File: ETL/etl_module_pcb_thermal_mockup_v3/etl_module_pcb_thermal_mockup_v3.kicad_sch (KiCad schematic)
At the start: 25 parts, among them J3 Conn_02x05_Counter_Clockwise, U1 ETROC_dummy_thermal_sensors, U2 ETROC_dummy_thermal_sensors, U3 ETROC_dummy_thermal_sensors, U4 ETROC_dummy_thermal_sensors, U5 ADC088SO22, U6 ADC088SO22, U7 ADC088SO22, U8 ADC088SO22

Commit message: Progress on etl_module_pcb_thermal_mockup_v3
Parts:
- removed C1, C3, C5, C7: 1.0uF, Capacitor_SMD:C_0201_0603Metric_Pad0.64x0.40mm_HandSolder, symbol Device:C
- removed C2, C4, C6, C8: 0.1uF, Capacitor_SMD:C_0201_0603Metric_Pad0.64x0.40mm_HandSolder, symbol Device:C
- removed RN1, RN2, RN3, RN4: 10k, Resistor_SMD:R_Array_Convex_8x0602, symbol Device:R_Pack08
- removed U5, U6, U7, U8: ADC088SO22, Package_SO:TSSOP-16_4.4x5mm_P0.65mm, symbol unl_silab:ADC088SO22
- added C?: 1uF, symbol Device:C
- added R? (x10): 40k, symbol Device:R
- added R?: 1M, symbol Device:R
- added RV?: 25k, symbol Device:R_Potentiometer
- added U?: AD780, Package_SO:SOIC-8_3.9x4.9mm_P1.27mm, symbol unl_silab:AD780
- added U?: AD77x8, Package_SO:SOIC-28W_7.5x18.7mm_P1.27mm, symbol unl_silab:AD77x8
- added Y?: 32kHz, symbol Device:Crystal
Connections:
- net +5V: now also C?.1, R?.1, R?.1, R?.1, R?.1, R?.1, R?.1, R?.1, R?.1, R?.1, U?.2 (+V_{IN}), U?.26 (DV_{DD}), U?.3 (AV_{DD})
- net CLK: now also U?.20 (SCLK)
- net DIN: now also U?.24 (DIN)
- net DOUT: now also U?.23 (DOUT)
- net GND: now also U1.11 (LGAD_BL+), U1.3 (ETROC_BLp), U2.11 (LGAD_BL+), U2.3 (ETROC_BLp), U3.11 (LGAD_BL+), U3.3 (ETROC_BLp), U4.11 (LGAD_BL+), U4.3 (ETROC_BLp), C?.2, R?.2, RV?.1, U?.14 (REFIN2(-)/AIN10), U?.17 (AGND), U?.25 (DGND), U?.4 (AGND), U?.4 (GND), U?.5 (REFIN1(-)); no longer U1.105 (LGAD_BR-), U1.108 (ETROC_TR-), U1.119 (ETROC_BR-), U1.12 (LGAD_BL-), U1.23 (LGAD_TL-), U1.5 (ETROC_BL-), U1.83 (LGAD_TR-), U1.9 (ETROC_TL-), U2.105 (LGAD_BR-), U2.108 (ETROC_TR-), U2.119 (ETROC_BR-), U2.12 (LGAD_BL-), U2.23 (LGAD_TL-), U2.5 (ETROC_BL-), U2.83 (LGAD_TR-), U2.9 (ETROC_TL-), U3.105 (LGAD_BR-), U3.108 (ETROC_TR-), U3.119 (ETROC_BR-), U3.12 (LGAD_BL-), U3.23 (LGAD_TL-), U3.5 (ETROC_BL-), U3.83 (LGAD_TR-), U3.9 (ETROC_TL-), U4.105 (LGAD_BR-), U4.108 (ETROC_TR-), U4.119 (ETROC_BR-), U4.12 (LGAD_BL-), U4.23 (LGAD_TL-), U4.5 (ETROC_BL-), U4.83 (LGAD_TR-), U4.9 (ETROC_TL-)
- net VCC: now also U3.1 (VCC), U4.1 (VCC); no longer U3.121 (VSS), U4.121 (VSS)
- net VSS: now also U3.121 (VSS), U4.121 (VSS); no longer U3.1 (VCC), U4.1 (VCC)
- net LGAD3: now reaches U3.104 (LGAD_BR+)
- net LGAD3: now also U3.83 (LGAD_TR-), U?.15 (AIN6)
- net at U3.107 (ETROC_TR+): now also U3.9 (ETROC_TL-)
- net ETROC3: now reaches U3.117 (ETROC_BR+)
- net ETROC3: now also U3.108 (ETROC_TR-), U?.11 (AIN5)
- net at U3.21 (LGAD_TL+): now also U3.12 (LGAD_BL-)
- net at U3.8 (ETROC_TL+): now also U3.5 (ETROC_BL-)
- net at U3.81 (LGAD_TR+): now also U3.23 (LGAD_TL-)
- net at U1.104 (LGAD_BR+): now also U1.83 (LGAD_TR-)
- net at U1.117 (ETROC_BR+): now also U1.108 (ETROC_TR-)
- net at U1.81 (LGAD_TR+): now also U1.23 (LGAD_TL-)
- net at U1.107 (ETROC_TR+): now also U1.9 (ETROC_TL-)
- net at U1.21 (LGAD_TL+): now also U1.12 (LGAD_BL-)
- net at U1.8 (ETROC_TL+): now also U1.5 (ETROC_BL-)
- net LGAD2: now reaches U2.104 (LGAD_BR+)
- net LGAD2: now also U2.83 (LGAD_TR-), U?.10 (AIN4)
- net ETROC2: now reaches U2.117 (ETROC_BR+)
- net ETROC2: now also U2.108 (ETROC_TR-), U?.9 (AIN3)
- net at U2.81 (LGAD_TR+): now also U2.23 (LGAD_TL-)
- net at U2.107 (ETROC_TR+): now also U2.9 (ETROC_TL-)
- net at U2.21 (LGAD_TL+): now also U2.12 (LGAD_BL-)
- net at U2.8 (ETROC_TL+): now also U2.5 (ETROC_BL-)
- net LGAD4: now reaches U4.104 (LGAD_BR+)
- net LGAD4: now also U4.83 (LGAD_TR-), U?.2 (AIN8)
- net ETROC4: now reaches U4.117 (ETROC_BR+)
- net ETROC4: now also U4.108 (ETROC_TR-), U?.1 (AIN7)
- net at U4.81 (LGAD_TR+): now also U4.23 (LGAD_TL-)
- net at U4.107 (ETROC_TR+): now also U4.9 (ETROC_TL-)
- net at U4.21 (LGAD_TL+): now also U4.12 (LGAD_BL-)
- net at U4.8 (ETROC_TL+): now also U4.5 (ETROC_BL-)
- net CS1: no longer names the net of J3.4 (Pin_4)
- net CS2 renamed ~{RDY}
- net ~{RDY}: now also U?.22 (~{RDY})
- net CS3 renamed ~{RESET}
- net ~{RESET}: now also U?.19 (~{RESET})
- net CS4 renamed CS
- net CS: now also U?.21 (~{CS})
- new net: R?.2, U3.105 (LGAD_BR-)
- new net: R?.2, U3.119 (ETROC_BR-)
- new net: R?.2, RV?.2
- new net: R?.2, U2.105 (LGAD_BR-)
- new net: R?.2, U2.119 (ETROC_BR-)
- new net: R?.2, U4.105 (LGAD_BR-)
- new net: R?.2, U4.119 (ETROC_BR-)
- new net: U?.27 (XTAL2), Y?.1
- new net: U?.28 (XTAL1), Y?.2
- new net 2.5V: R?.1, RV?.3, U?.13 (REFIN2(+)/AIN9), U?.5 (TRIM)
- new net ETROC1: R?.2, U1.119 (ETROC_BR-), U?.7 (AIN1)
- new net LGAD1: R?.2, U1.105 (LGAD_BR-), U?.8 (AIN2)
- new net V_{ref}: R?.1, R?.2, U?.12 (AINCOM), U?.6 (REFIN1(+))
- no-connect marks 0 -> 6
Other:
- note added: "*(Optional)* Populate 2.5V reference for absolute (vs ratiometric)measurements."
- note added: "Single Resistance: R = 34.6 * T [C] + 9600 Four in Series: R_{ser} = 4*R = 138.4 * T [C] + 38400 V_{sense} = V * (R_{ser} / (R_{ser} + 40k)) -> 4.5mV/[C] near T=0 [C]"
- note removed: "TODO: Wire up power to pin header Wire up power to b2b connector Wire up readout to pin header Wier up readout to b2b connector Add pin header for ETROC heater power supply"
- moved on the sheet: U1, U2, U3, U4

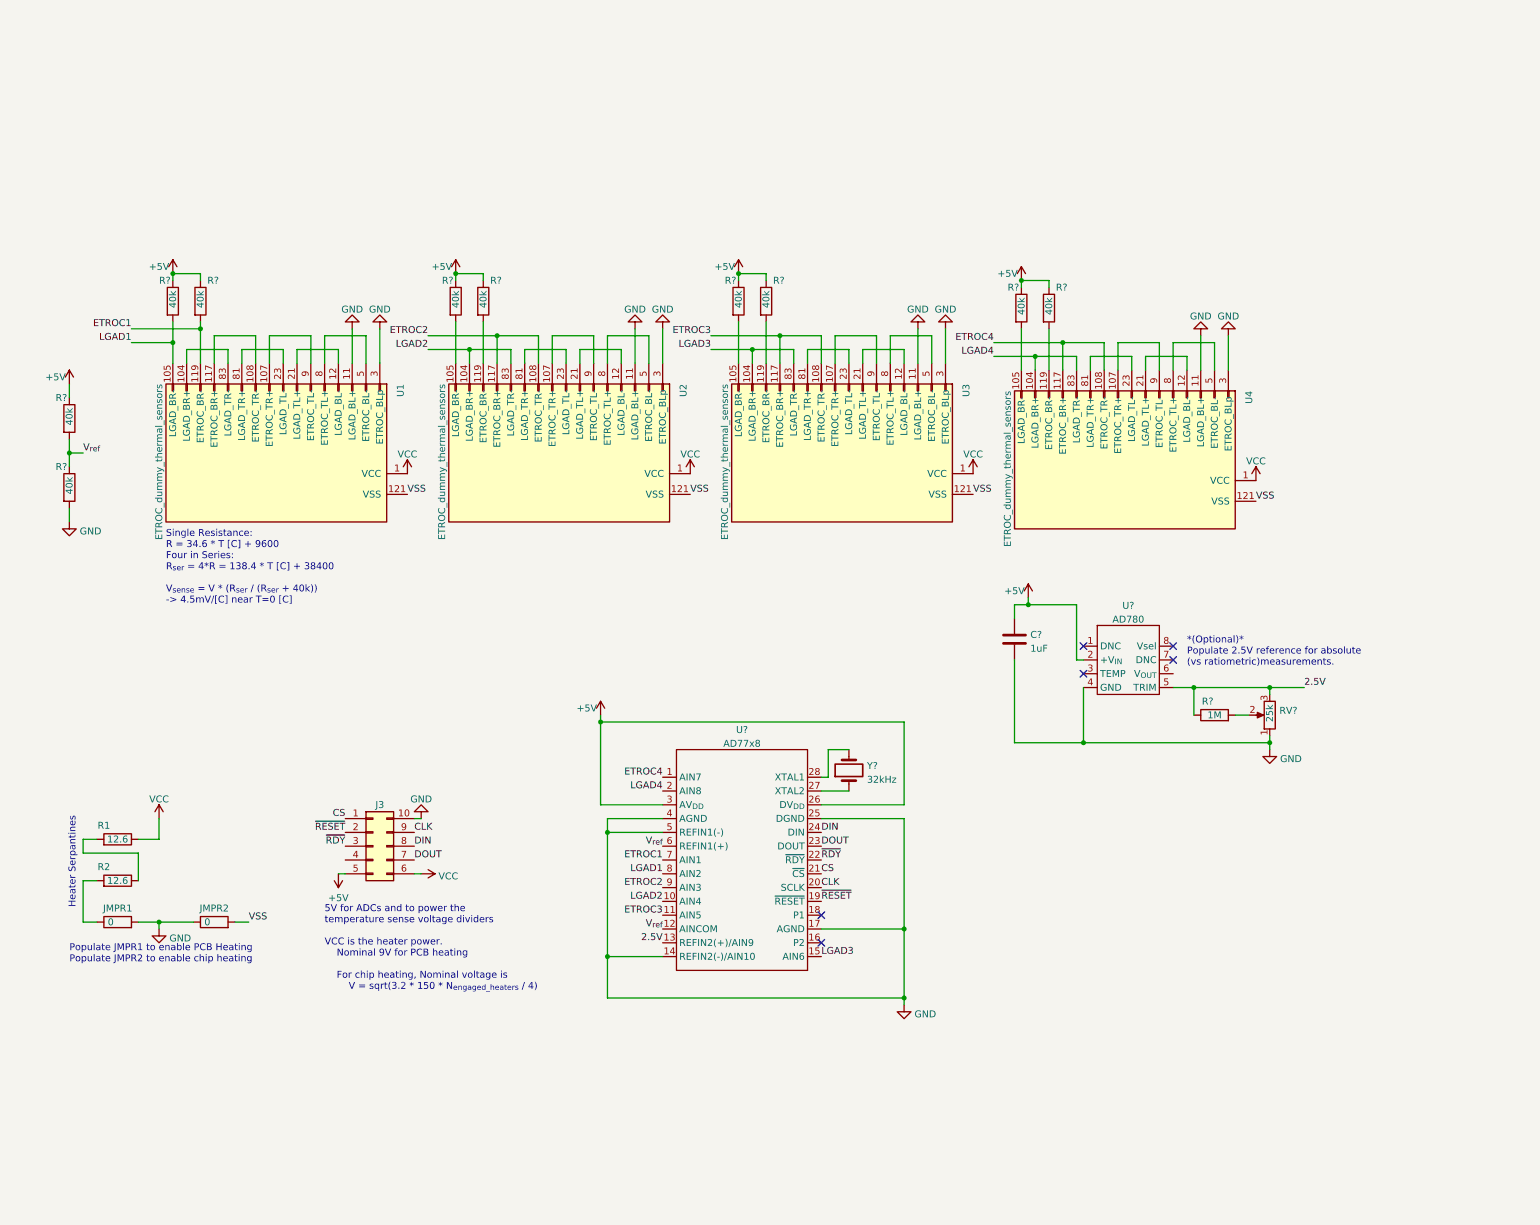
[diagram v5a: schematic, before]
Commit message: Work on etl_module_pcb_thermal_mockup_v3
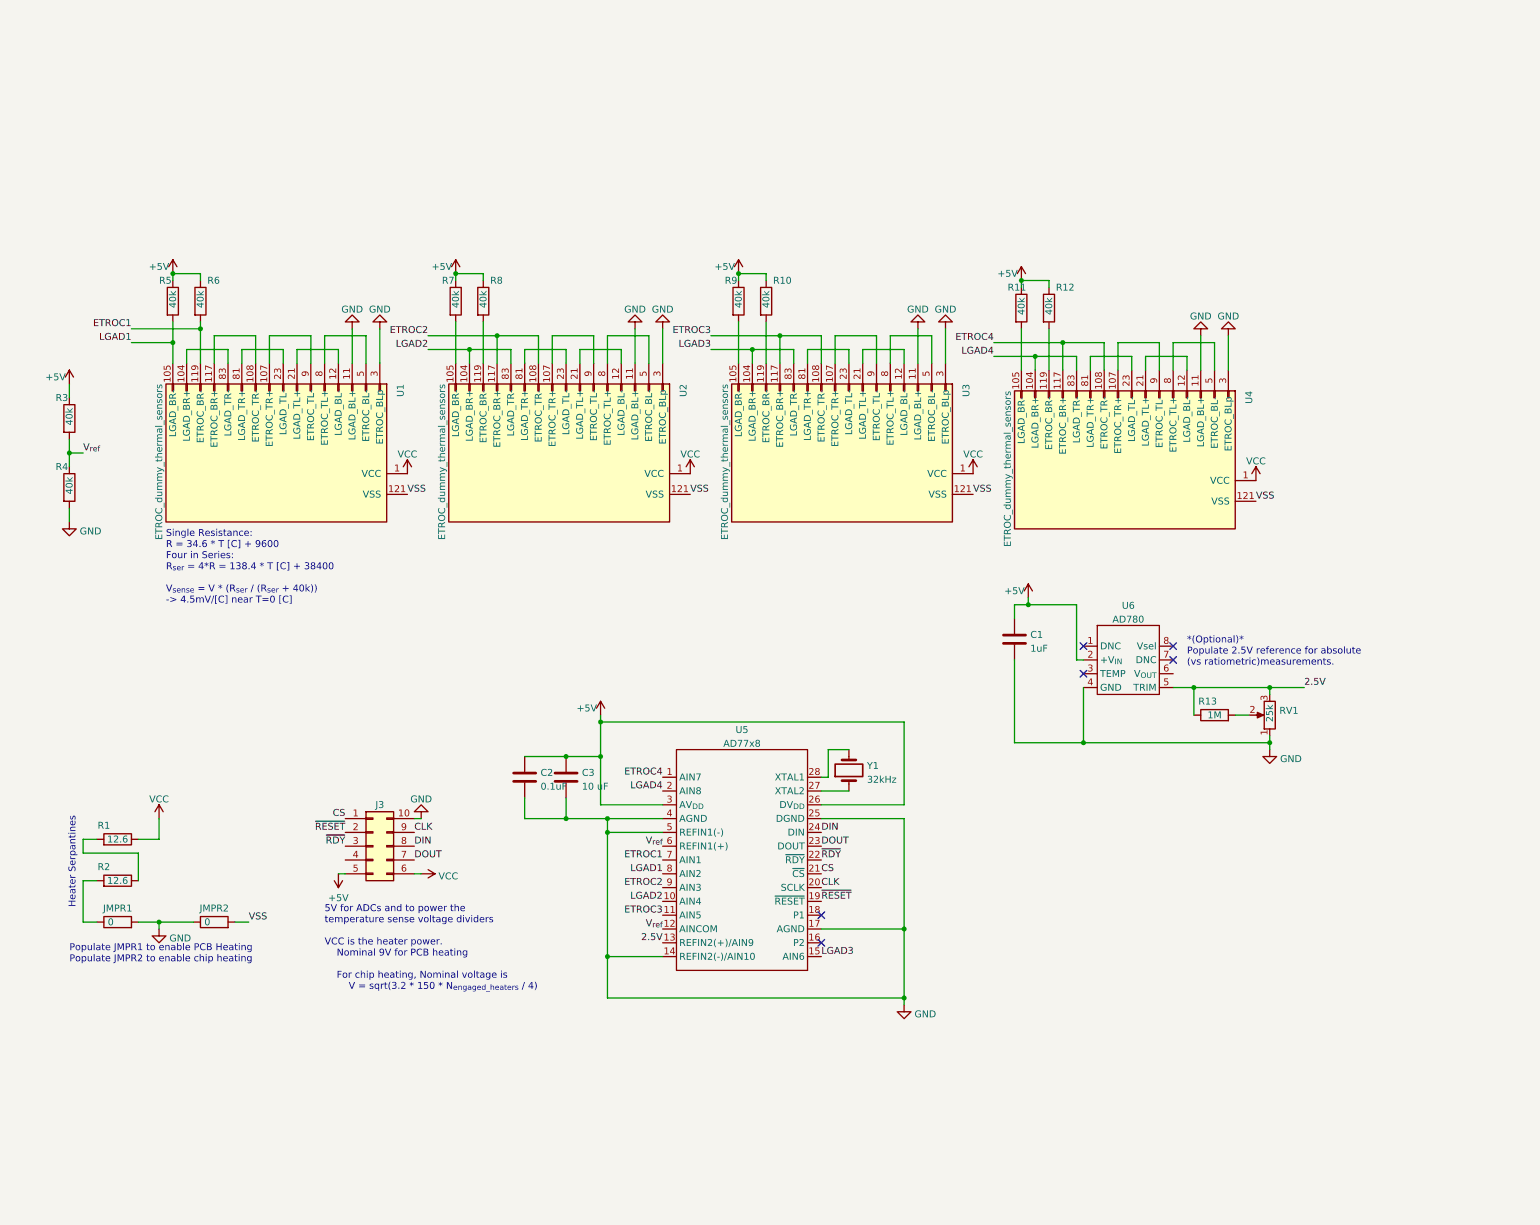
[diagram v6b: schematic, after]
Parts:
- added C2: 0.1uF, Capacitor_SMD:C_0805_2012Metric_Pad1.18x1.45mm_HandSolder, symbol Device:C
- added C3: 10 uF, Capacitor_SMD:C_0805_2012Metric_Pad1.18x1.45mm_HandSolder, symbol Device:C
- C1: renamed from C?; footprint (none) -> Capacitor_SMD:C_0805_2012Metric_Pad1.18x1.45mm_HandSolder
- R10, R11, R12, R13, R3, R4, R5, R6, R7, R8, R9: renamed from R?; footprint (none) -> Resistor_SMD:R_0805_2012Metric_Pad1.20x1.40mm_HandSolder
- RV1: renamed from RV?; footprint (none) -> Potentiometer_SMD:Potentiometer_Bourns_3224W_Vertical
- Y1: renamed from Y?; footprint (none) -> Crystal:Crystal_SMD_3215-2Pin_3.2x1.5mm
- gave numbers to parts that had none: 2
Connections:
- net +5V: now also C2.1, C3.1
- net GND: now also C2.2, C3.2

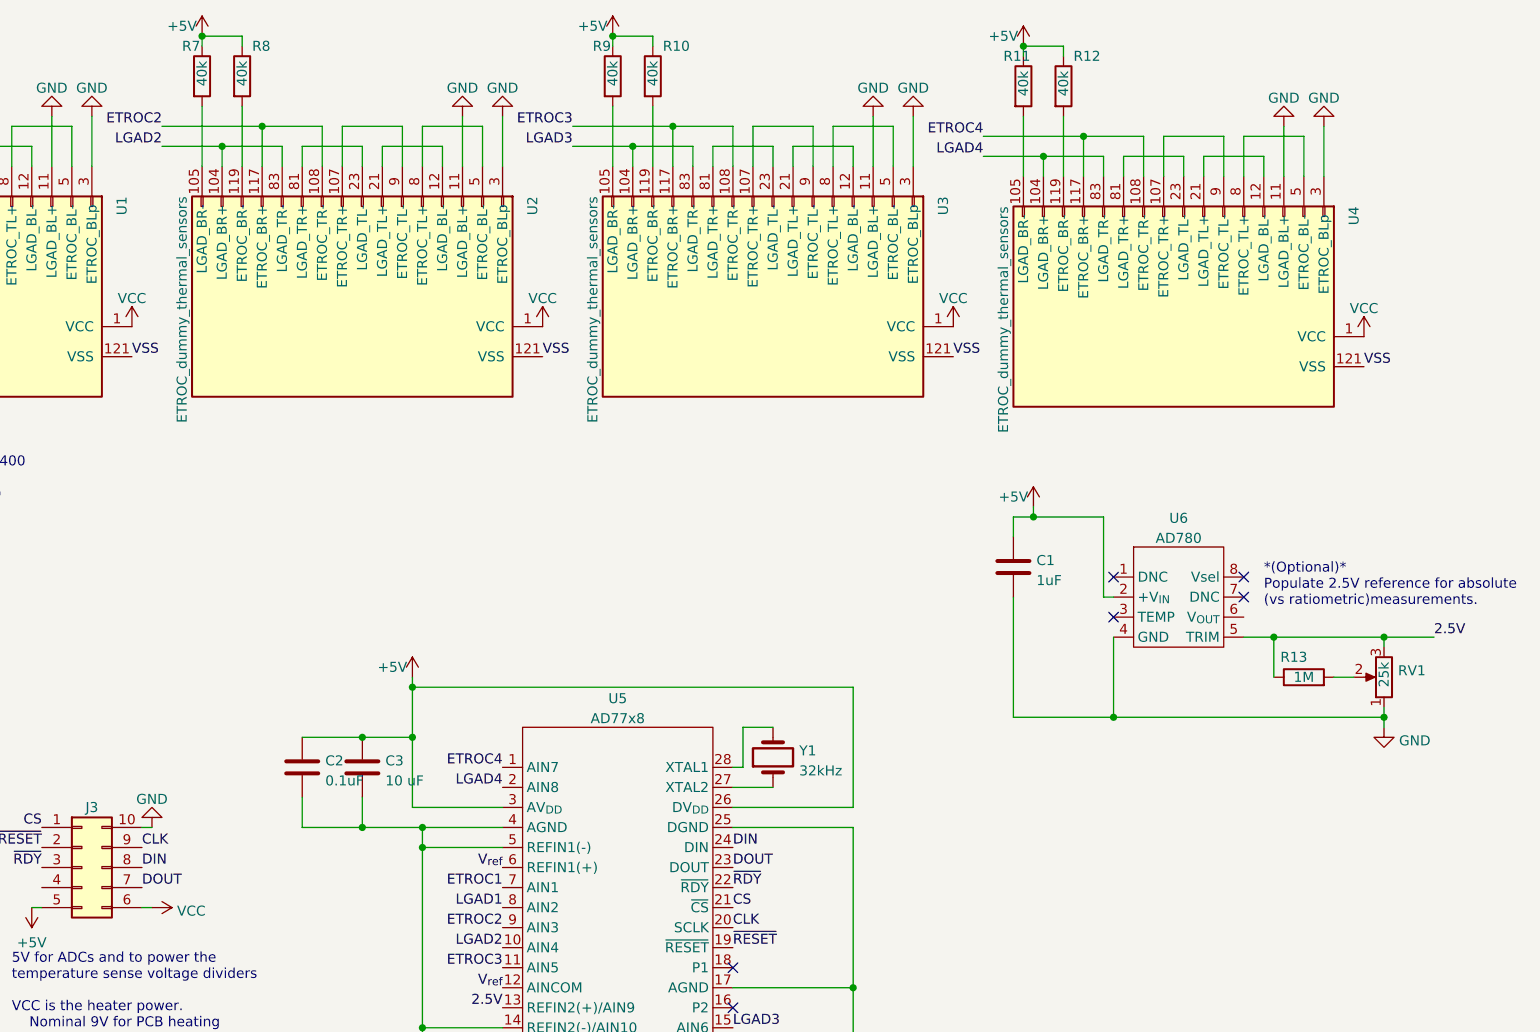
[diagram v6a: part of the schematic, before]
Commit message: Almost finished routing on etl_module_pcb_thermal_mockup_v3
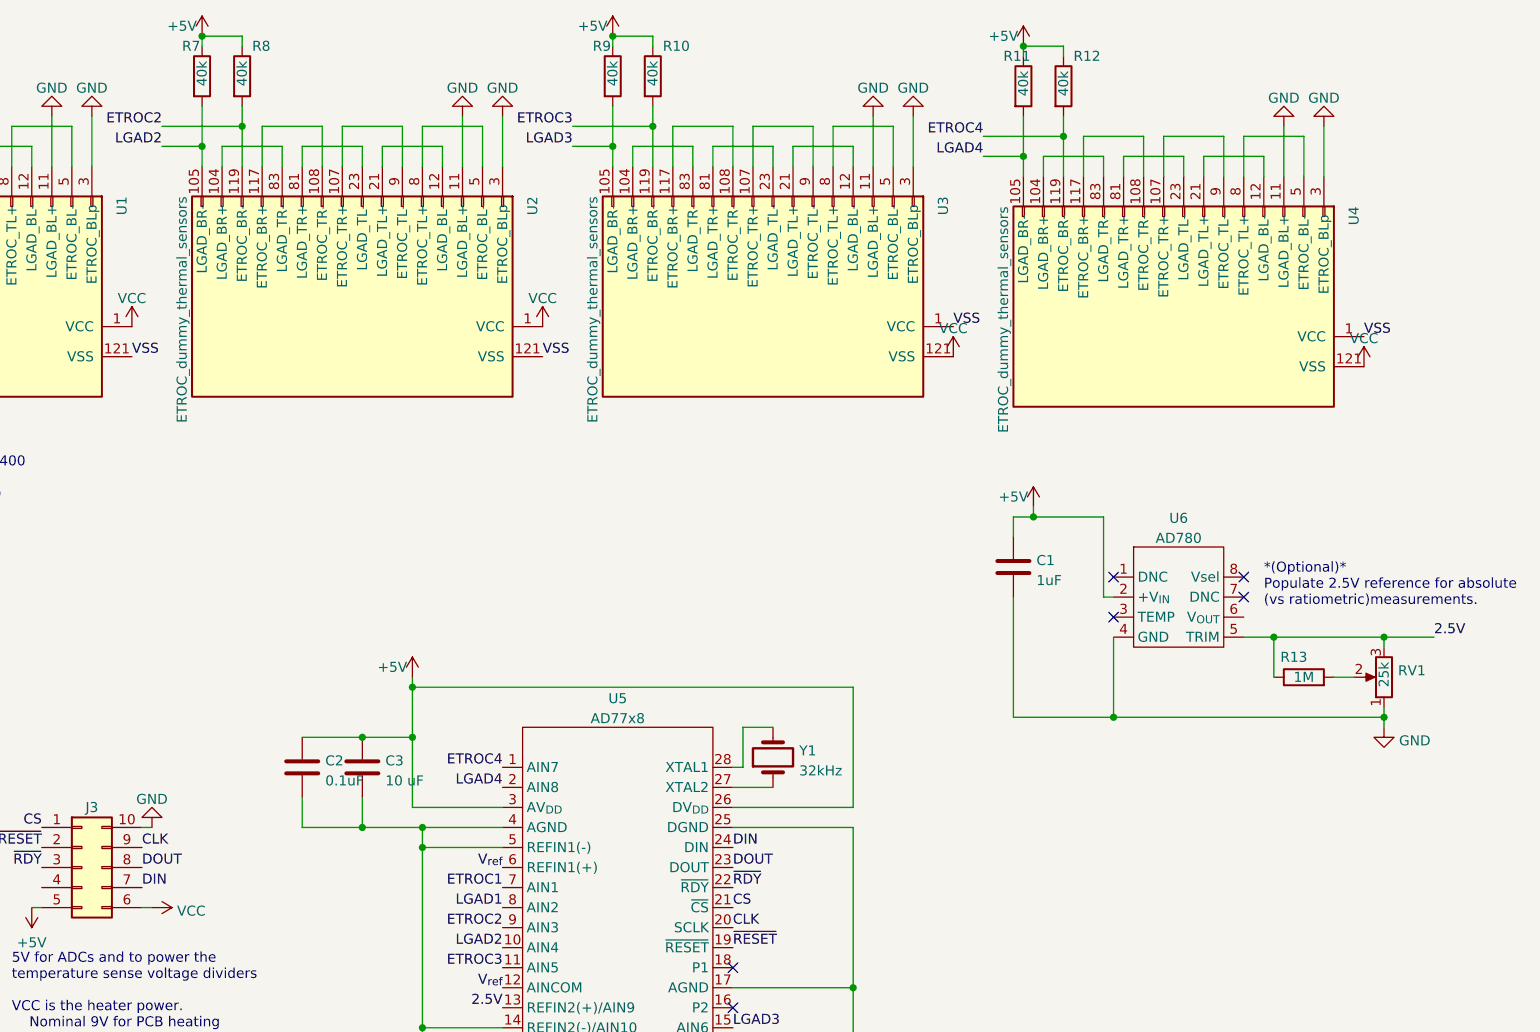
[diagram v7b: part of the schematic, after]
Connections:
- net DIN: now also J3.7 (Pin_7); no longer J3.8 (Pin_8)
- net DOUT: now also J3.8 (Pin_8); no longer J3.7 (Pin_7)
- net ETROC2: now also R8.2, U2.119 (ETROC_BR-); no longer U2.108 (ETROC_TR-), U2.117 (ETROC_BR+)
- net ETROC3: now also R10.2, U3.119 (ETROC_BR-); no longer U3.108 (ETROC_TR-), U3.117 (ETROC_BR+)
- net ETROC4: now also R12.2, U4.119 (ETROC_BR-); no longer U4.108 (ETROC_TR-), U4.117 (ETROC_BR+)
- net LGAD2: now also R7.2, U2.105 (LGAD_BR-); no longer U2.104 (LGAD_BR+), U2.83 (LGAD_TR-)
- net LGAD3: now also R9.2, U3.105 (LGAD_BR-); no longer U3.104 (LGAD_BR+), U3.83 (LGAD_TR-)
- net LGAD4: now also R11.2, U4.105 (LGAD_BR-); no longer U4.104 (LGAD_BR+), U4.83 (LGAD_TR-)
- net VCC: now also U3.121 (VSS), U4.121 (VSS); no longer U3.1 (VCC), U4.1 (VCC)
- net VSS: now also U3.1 (VCC), U4.1 (VCC); no longer U3.121 (VSS), U4.121 (VSS)
- new net: U3.104 (LGAD_BR+), U3.83 (LGAD_TR-)
- new net: U3.108 (ETROC_TR-), U3.117 (ETROC_BR+)
- new net: U2.104 (LGAD_BR+), U2.83 (LGAD_TR-)
- new net: U2.108 (ETROC_TR-), U2.117 (ETROC_BR+)
- new net: U4.104 (LGAD_BR+), U4.83 (LGAD_TR-)
- new net: U4.108 (ETROC_TR-), U4.117 (ETROC_BR+)

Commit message: Finishes layout
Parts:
- added 2.5V1, 5V1, E1, E2, E3, E4, GND1, L1, L2, L3, L4, VCC1: TestPoint, TestPoint:TestPoint_Pad_1.0x1.0mm, symbol Connector:TestPoint
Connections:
- net +5V: now also J3.6 (Pin_6), 5V1.1; no longer J3.5 (Pin_5)
- net 2.5V: now also 2.5V1.1
- net ETROC1: now also U5.9 (AIN3), E1.1; no longer U5.7 (AIN1)
- net ETROC2: now also U5.11 (AIN5), E2.1; no longer U5.9 (AIN3)
- net ETROC3: now also U5.7 (AIN1), E3.1; no longer U5.11 (AIN5)
- net ETROC4: now also U5.2 (AIN8), E4.1; no longer U5.1 (AIN7)
- net GND: now also GND1.1
- net LGAD1: now also L1.1
- net LGAD2: now also L2.1
- net LGAD3: now also L3.1
- net LGAD4: now also U5.1 (AIN7), L4.1; no longer U5.2 (AIN8)
- net VCC: now also J3.5 (Pin_5), VCC1.1; no longer J3.6 (Pin_6)
